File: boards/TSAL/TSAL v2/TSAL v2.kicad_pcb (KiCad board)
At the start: 2 copper layers, 25 parts, among them J1 Ultrafit_2, J2 Ultrafit_2, J3 micromatch_female_RA_4, Q1 NMOS_GSD_30V, U1 LR8K4-G, U2 ZXRE160, U3 MCP6001RT, U4 LTV-356T

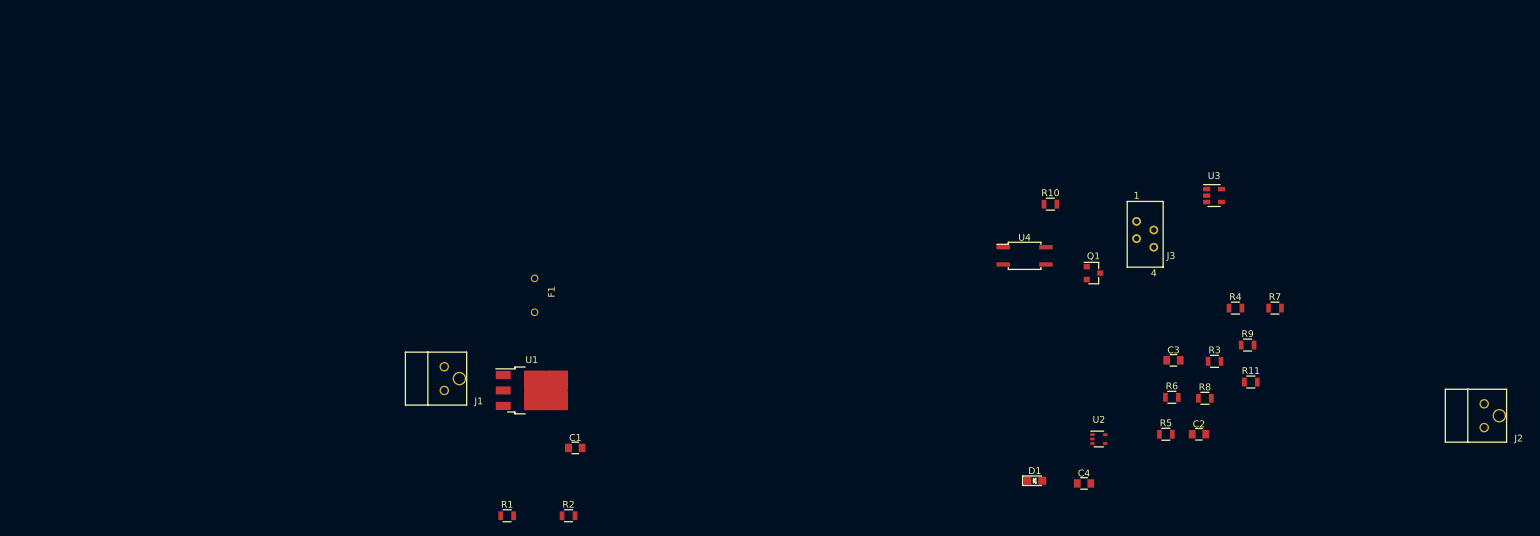
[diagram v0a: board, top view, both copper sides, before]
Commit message: Adding TSAL v2 final schematic
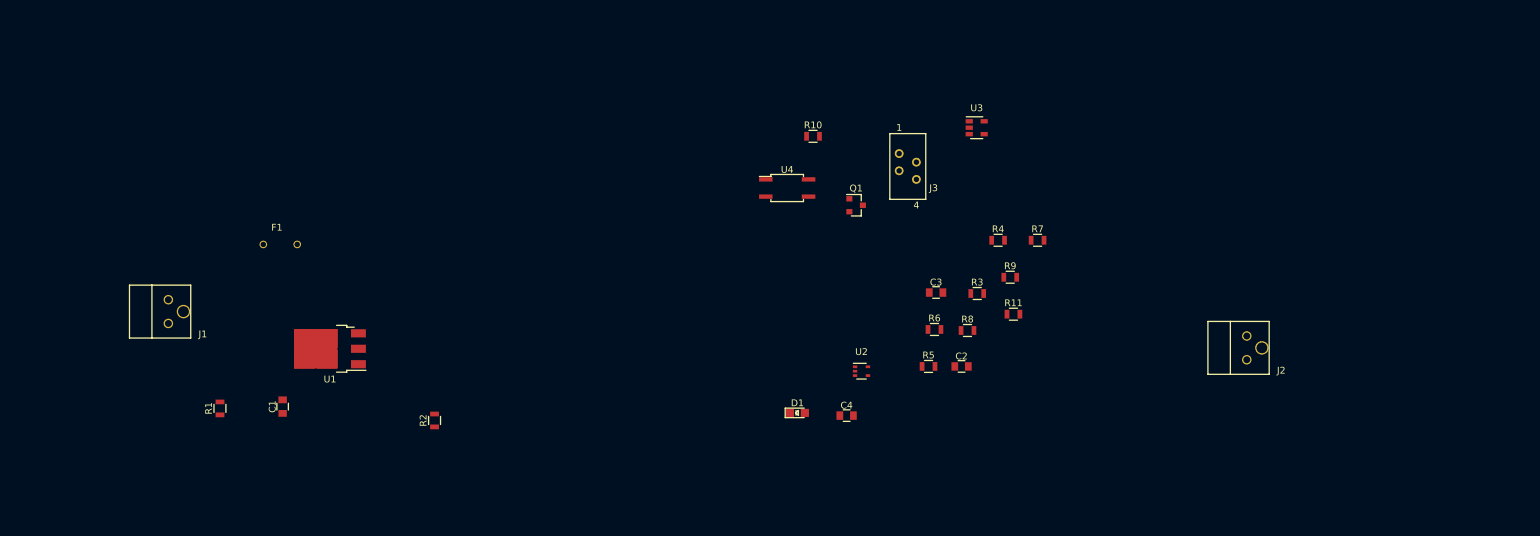
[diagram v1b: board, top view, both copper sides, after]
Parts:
- moved R1 45.2 mm to (73.6, 119.2), turned to 90 degrees
- moved C1 43.6 mm to (82.8, 118.9), turned to 90 degrees
- moved J1 41.9 mm to (66.0, 103.2)
- moved C4 36.4 mm to (166.0, 120.2)
- moved D1 36.4 mm to (158.7, 119.8)
- moved C2 36.4 mm to (182.9, 113.0)
- moved C3 36.4 mm to (179.2, 102.1)
- moved F1 36.4 mm to (85.0, 95.0), turned to 180 degrees
- moved J2 36.4 mm to (225.0, 108.5)
- moved J3 36.4 mm to (173.8, 86.7)
- moved Q1 36.4 mm to (167.4, 89.2)
- moved R10 36.4 mm to (161.1, 79.1)
- moved R11 36.4 mm to (190.6, 105.3)
- moved R3 36.4 mm to (185.3, 102.2)
- moved R4 36.4 mm to (188.3, 94.4)
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
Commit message: BOM, Netlist, PCB final
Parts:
- added G***: LOGO, footprints:Olin_O, B.Cu at (50.8, 72.4)
- added G***: LOGO, footprints:Logo_Large, B.Cu at (80.0, 99.1)
- J3: value micromatch_female_RA_4 -> micromatch_female_TOP_ENTRY_locking_4; footprint footprints:micromatch_female_ra_4 -> footprints:micromatch_female_vert_4
- moved J2 152.5 mm to (73.0, 96.0), turned to 180 degrees
- moved R7 137.1 mm to (57.1, 98.7), turned to 90 degrees
- moved R4 136.3 mm to (52.1, 94.0), turned to 270 degrees
- moved R3 133.2 mm to (52.1, 98.7), turned to 270 degrees
- moved U3 125.2 mm to (61.0, 93.8), turned to 270 degrees
- moved R9 123.7 mm to (67.0, 88.0)
- moved R11 123.6 mm to (71.9, 70.7)
- moved R6 122.6 mm to (57.1, 94.0), turned to 90 degrees
- moved R5 118.0 mm to (61.0, 98.7), turned to 90 degrees
- moved R8 111.6 mm to (72.4, 101.6)
- moved J3 108.5 mm to (66.8, 68.2), turned to 90 degrees
- moved C3 105.6 mm to (73.7, 104.4), turned to 270 degrees
- moved C4 102.9 mm to (66.5, 93.9), turned to 90 degrees
- moved R10 102.4 mm to (59.2, 89.2), turned to 270 degrees
- moved C2 102.2 mm to (81.3, 102.4), turned to 90 degrees
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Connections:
- C1 pad 2: GND -> TS-
- U4 pad 4: VCC -> GLV+
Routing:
- net TS-: track 0.00 -> 105.9 mm, vias 0 -> 2
- net /5V_TS: track 0.00 -> 41.0 mm, vias 0 -> 25
- net Net-(R8-Pad2): track 0.00 -> 23.4 mm, vias 0 -> 2
- net Net-(D1-Pad2): track 0.00 -> 17.1 mm
- net TS+: track 0.00 -> 14.4 mm
- net Net-(R5-Pad1): track 0.00 -> 13.2 mm
- net GLV+: track 0.00 -> 11.2 mm
- net Net-(R10-Pad1): track 0.00 -> 10.4 mm
- net Net-(Q1-Pad1): track 0.00 -> 9.41 mm
- net Net-(F1-Pad2): track 0.00 -> 9.25 mm
- net TSAL-: track 0.00 -> 6.61 mm
- net Net-(R1-Pad1): track 0.00 -> 5.99 mm
- net GND: track 0.00 -> 5.96 mm, vias 0 -> 1
- net Net-(R4-Pad1): track 0.00 -> 5.08 mm
- net Net-(D1-Pad1): track 0.00 -> 3.96 mm
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- added copper zone on B.Cu, net /5V_TS
- added copper zone on B.Cu, net GND
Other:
- board outline added: 40.6 x 58.4 mm
- net class Default: clearance 0.2 -> 0.1524; trace_width 0.25 -> 0.254; via_dia 0.6 -> 0.6096; via_drill 0.4 -> 0.3048
- rule trace_clearance: 0.2 -> 0.1524
- rule via_min_drill: 0.3 -> 0.3048
- rule via_min_size: 0.4 -> 0.6096
- board text added: "HV"
- board text added: "LV"
- board text added: "TS-"
- board text added: "TSAL Rev 2.0 Utsav Gupta 2/5/2018"

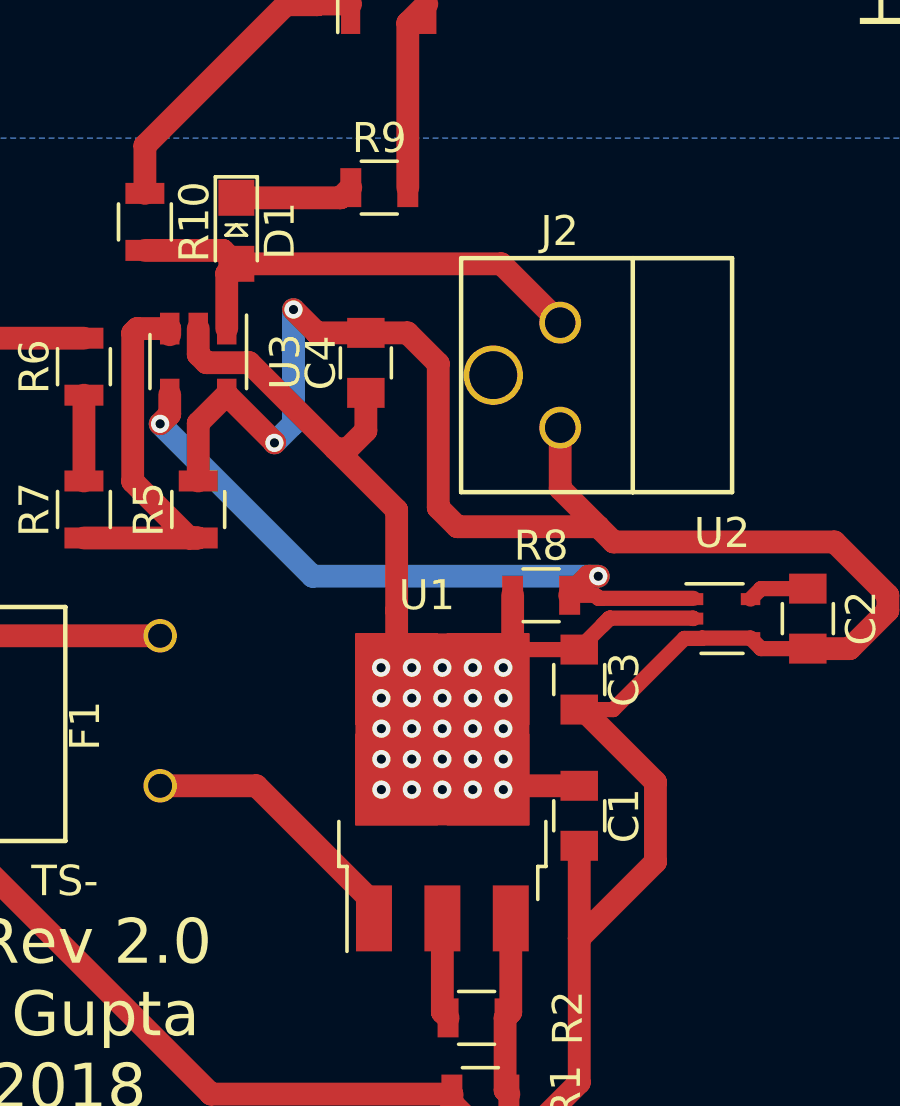
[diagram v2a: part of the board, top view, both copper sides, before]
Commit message: Solved 2 errors
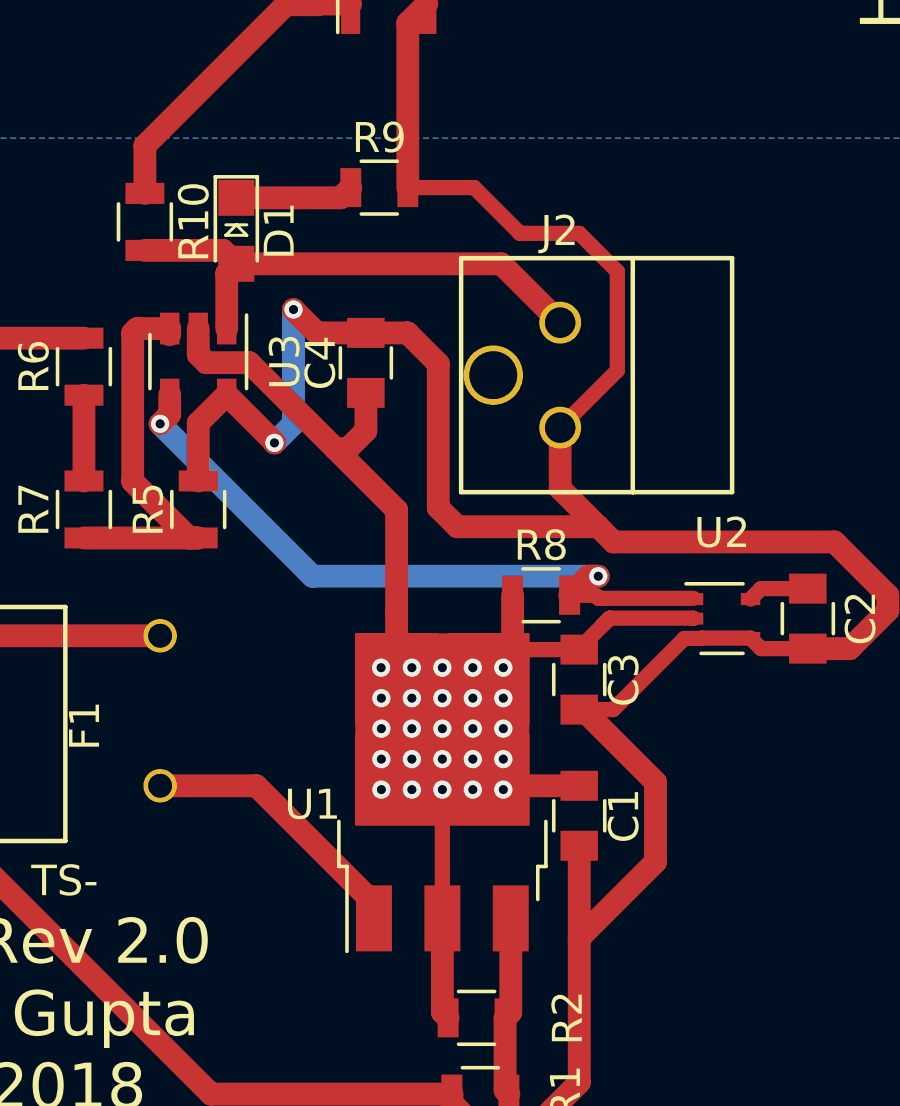
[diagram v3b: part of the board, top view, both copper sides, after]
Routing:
- net TS-: track 105.9 -> 120.1 mm
- net /5V_TS: track 41.0 -> 45.2 mm
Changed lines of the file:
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@@
   (general
     (links 49)
-    (no_connects 5)
+    (no_connects 0)
     (area 42.644287 59.102172 90.170001 123.190001)
     (thickness 1.6)
     (drawings 14)
-    (tracks 157)
+    (tracks 165)
     (zones 0)
     (modules 27)
@@
   )
   (setup
-    (last_trace_width 0.762)
+    (last_trace_width 0.508)
     (user_trace_width 0.254)
     (user_trace_width 0.508)
@@
     (tags "DPAK TO-252 DPAK-3 TO-252-3 SOT-428")
     (attr smd)
-    (fp_text reference U1 (at 6.569335 -0.517787 180) (layer F.SilkS)
+    (fp_text reference U1 (at -0.415665 -4.327787 180) (layer F.SilkS)
       (effects (font (size 1 1) (thickness 0.15)))
     )
@@
   (gr_line (start 46.99 121.92) (end 85.09 121.92) (layer Edge.Cuts) (width 0.15))
   (gr_line (start 45.72 64.77) (end 45.72 120.65) (layer Edge.Cuts) (width 0.15))
+  (segment (start 69.097787 112.369335) (end 69.097787 108.078335) (width 0.508) (layer F.Cu) (net 1))
+  (segment (start 69.097787 108.078335) (end 69.096787 108.077335) (width 0.508) (layer F.Cu) (net 1))
   (segment (start 62.661721 93.846599) (end 65.532 96.716878) (width 0.762) (layer F.Cu) (net 1))
   (segment (start 65.532 96.716878) (end 67.572787 98.757665) (width 0.762) (layer F.Cu) (net 1))
@@
   (via (at 74.93 69.85) (size 0.6096) (drill 0.3048) (layers F.Cu B.Cu) (net 2))
   (segment (start 72.898 70.739) (end 72.898 67.183) (width 0.762) (layer F.Cu) (net 2))
+  (segment (start 74.93 90.805) (end 74.93 94.107) (width 0.508) (layer F.Cu) (net 3))
+  (segment (start 74.93 94.107) (end 73.025 96.012) (width 0.508) (layer F.Cu) (net 3))
+  (segment (start 73.66 89.535) (end 74.93 90.805) (width 0.508) (layer F.Cu) (net 3))
+  (segment (start 71.683254 89.535) (end 73.66 89.535) (width 0.508) (layer F.Cu) (net 3))
+  (segment (start 67.945 88.011) (end 70.159254 88.011) (width 0.508) (layer F.Cu) (net 3))
+  (segment (start 70.159254 88.011) (end 71.683254 89.535) (width 0.508) (layer F.Cu) (net 3))
   (segment (start 63.5 96.52) (end 63.5 96.5) (width 0.762) (layer F.Cu) (net 3))
   (segment (start 63.5 96.5) (end 61.91 94.91) (width 0.762) (layer F.Cu) (net 3))

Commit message: Hopefully finalised
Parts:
- moved G*** 5.72 mm to (80.0, 93.3)
- moved G*** 5.24 mm to (49.5, 77.5)
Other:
- outline, holes or cut-outs redrawn
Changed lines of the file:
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@@
     (area 42.644287 59.102172 90.170001 123.190001)
     (thickness 1.6)
-    (drawings 14)
+    (drawings 18)
     (tracks 165)
     (zones 0)
@@
       (effects (font (size 1 1) (thickness 0.15)))
     )
-    (fp_text value NMOS_GSD_30V (at -0.03 -2.55 90) (layer F.Fab)
+    (fp_text value NMOS_GSD_30V (at -3.032 -16.068 90) (layer F.Fab)
       (effects (font (size 1 1) (thickness 0.15)))
     )
@@
   )
   (module footprints:Olin_O (layer B.Cu)
-    (at 50.8 72.39 90)
+    (at 49.53 77.47 90)
     (fp_text reference G*** (at 10.16 5.08 90) (layer B.SilkS) hide
       (effects (font (thickness 0.3)) (justify mirror))
@@
   )
   (module footprints:Logo_Large (layer B.Cu)
-    (at 80.01 99.06 270)
+    (at 80.01 93.345 270)
     (fp_text reference G*** (at 0 0 270) (layer B.SilkS) hide
       (effects (font (thickness 0.3)) (justify mirror))
@@
       (xy 18.232145 4.0226) (xy 18.481106 4.090329) (xy 18.746513 4.111367) (xy 18.846075 4.107132)) (layer B.SilkS) (width 0.01))
   )
+  (gr_arc (start 81.28 117.285008) (end 81.28 121.285) (angle -90) (layer Edge.Cuts) (width 0.1))
+  (gr_line (start 48.639984 121.285) (end 81.28 121.285) (layer Edge.Cuts) (width 0.1))
+  (gr_arc (start 81.28 66.864992) (end 85.279992 66.864992) (angle -90) (layer Edge.Cuts) (width 0.1))
+  (gr_arc (start 48.639984 66.864992) (end 48.639984 62.865) (angle -90) (layer Edge.Cuts) (width 0.1))
+  (gr_line (start 85.279992 117.285008) (end 85.279992 66.864992) (layer Edge.Cuts) (width 0.1))
+  (gr_arc (start 48.639984 117.285008) (end 44.639992 117.285008) (angle -90) (layer Edge.Cuts) (width 0.1))
+  (gr_circle (center 48.639984 117.285008) (end 48.639984 115.285012) (layer Edge.Cuts) (width 0.1))
+  (gr_circle (center 48.639984 66.864992) (end 48.639984 64.864996) (layer Edge.Cuts) (width 0.1))
+  (gr_circle (center 81.28 117.285008) (end 81.28 115.285012) (layer Edge.Cuts) (width 0.1))
+  (gr_line (start 44.639992 66.864992) (end 44.639992 117.285008) (layer Edge.Cuts) (width 0.1))
+  (gr_circle (center 81.28 66.864992) (end 81.28 64.864996) (layer Edge.Cuts) (width 0.1))
+  (gr_line (start 81.28 62.865) (end 48.639984 62.865) (layer Edge.Cuts) (width 0.1))
   (gr_text TS- (at 56.515 111.125) (layer F.SilkS)
     (effects (font (size 1.016 1.016) (thickness 0.254)))
   )
-  (gr_text "TSAL Rev 2.0\nUtsav Gupta\n2/5/2018\n" (at 54.61 115.57) (layer F.SilkS)
+  (gr_text "TSAL Rev 2.0\nUtsav Gupta\n2/5/2018\n" (at 57.785 116.205) (layer F.SilkS)
     (effects (font (size 1.5 1.5) (thickness 0.3)))
   )
-  (gr_arc (start 46.99 120.65) (end 46.99 121.92) (angle 90) (layer Edge.Cuts) (width 0.15))
-  (gr_arc (start 85.09 120.65) (end 86.36 120.65) (angle 90) (layer Edge.Cuts) (width 0.15))
-  (gr_arc (start 85.09 64.77) (end 85.09 63.5) (angle 90) (layer Edge.Cuts) (width 0.15))
-  (gr_arc (start 46.99 64.77) (end 45.72 64.77) (angle 90) (layer Edge.Cuts) (width 0.15))
   (dimension 12.7 (width 0.3) (layer F.SilkS)
     (gr_text "0.5000 in" (at 48.18 78.563549 270) (layer F.SilkS)
@@
     (effects (font (size 1.5 1.5) (thickness 0.3)))
   )
-  (gr_line (start 48.26 78.74) (end 86.36 78.74) (layer F.SilkS) (width 0.2))
-  (gr_line (start 85.09 63.5) (end 46.99 63.5) (layer Edge.Cuts) (width 0.15))
-  (gr_line (start 86.36 120.65) (end 86.36 64.77) (layer Edge.Cuts) (width 0.15))
-  (gr_line (start 46.99 121.92) (end 85.09 121.92) (layer Edge.Cuts) (width 0.15))
-  (gr_line (start 45.72 64.77) (end 45.72 120.65) (layer Edge.Cuts) (width 0.15))
+  (gr_line (start 46.355 78.74) (end 84.455 78.74) (layer F.SilkS) (width 0.2))
   (segment (start 69.097787 112.369335) (end 69.097787 108.078335) (width 0.508) (layer F.Cu) (net 1))
   (segment (start 69.097787 108.078335) (end 69.096787 108.077335) (width 0.508) (layer F.Cu) (net 1))

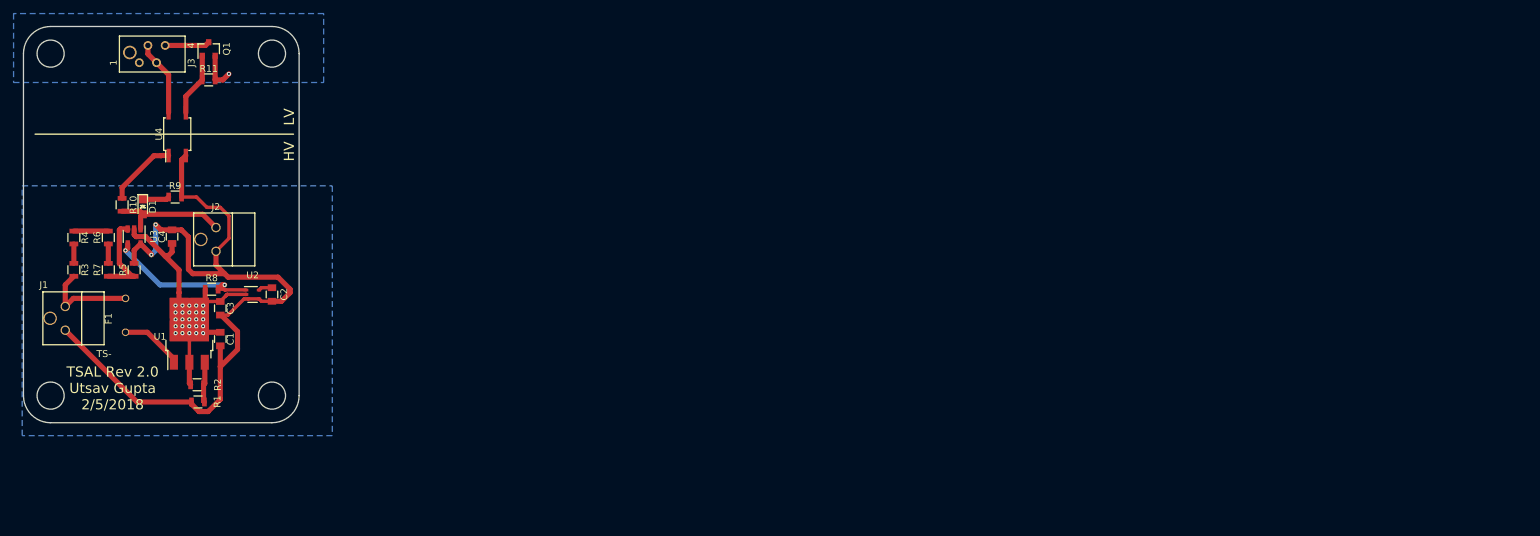
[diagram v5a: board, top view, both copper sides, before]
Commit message: Added 1.43k res for AIL
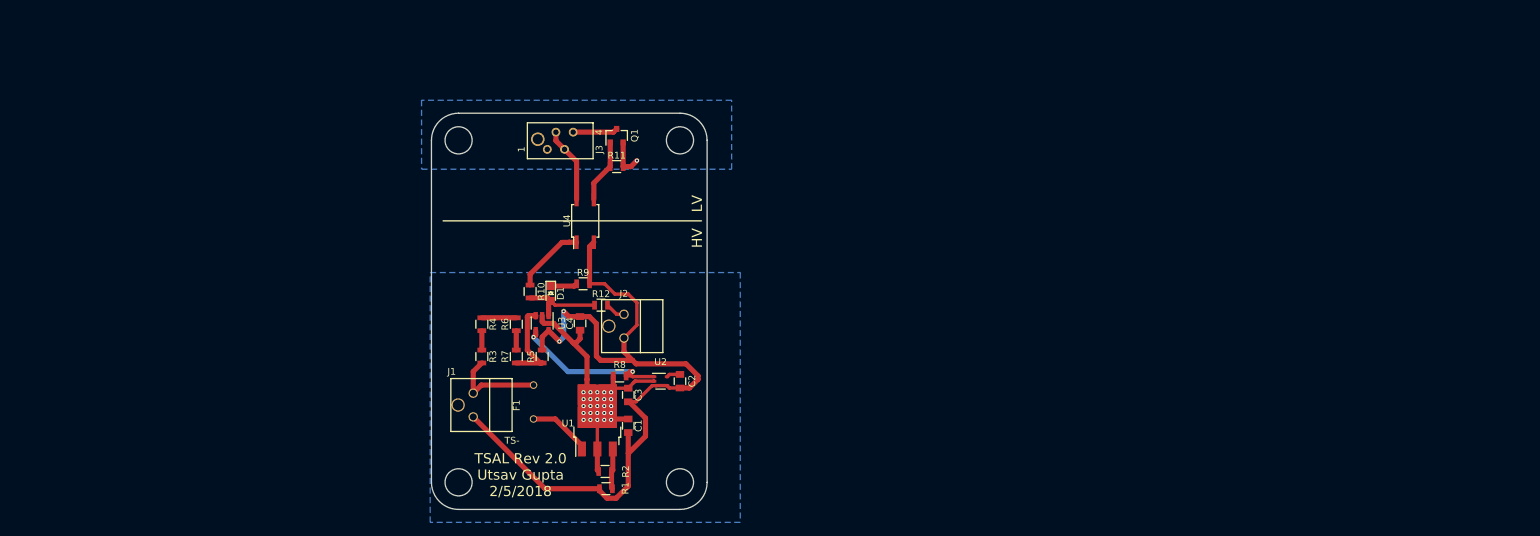
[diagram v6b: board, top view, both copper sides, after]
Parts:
- added R12: R_1.43k, footprints:R_0805_OEM, F.Cu at (129.8, 103.9)
- moved R11 61.5 mm to (132.1, 83.5)
- moved R2 61.5 mm to (130.4, 128.5)
- moved R8 61.5 mm to (132.5, 114.4)
- moved U1 61.5 mm to (129.2, 121.0)
- moved D1 61.5 mm to (122.4, 102.2)
- moved R3 61.5 mm to (112.2, 111.5)
- moved R4 61.5 mm to (112.2, 106.8)
- moved R6 61.5 mm to (117.3, 106.8)
- moved R7 61.5 mm to (117.3, 111.5)
- moved C1 61.5 mm to (133.8, 121.7)
- moved C2 61.5 mm to (141.4, 115.2)
- moved C3 61.5 mm to (133.8, 117.2)
- moved C4 61.5 mm to (126.7, 106.6)
- moved F1 61.5 mm to (119.8, 115.7)
- moved G*** 61.5 mm to (109.7, 90.3)
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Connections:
- J2 pad 1: Net-(D1-Pad2) -> Net-(J2-Pad1)
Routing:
- net Net-(D1-Pad2): track 17.1 -> 12.2 mm
- net Net-(J2-Pad1): track 0.00 -> 2.99 mm

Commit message: Forgot to save the file
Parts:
- moved Q1 59.3 mm to (178.1, 116.4), turned to 0 degrees
- moved J3 57.7 mm to (176.1, 111.2), turned to 0 degrees
- moved G*** 57.2 mm to (166.8, 94.0), turned to 0 degrees
- moved R11 52.9 mm to (173.5, 116.4), turned to 270 degrees
- moved U4 43.1 mm to (165.5, 111.7), turned to 0 degrees
- moved R4 39.4 mm to (150.3, 96.5), turned to 180 degrees
- moved R3 36.5 mm to (145.5, 96.5), turned to 180 degrees
- moved J1 36.0 mm to (136.6, 95.2), turned to 90 degrees
- moved R10 35.8 mm to (155.1, 103.6), turned to 180 degrees
- moved R6 33.4 mm to (150.3, 101.6), turned to 0 degrees
- moved D1 32.7 mm to (154.8, 106.7), turned to 180 degrees
- moved R9 31.0 mm to (156.3, 111.4), turned to 270 degrees
- moved R7 29.9 mm to (145.5, 101.6), turned to 0 degrees
- moved U3 29.4 mm to (150.5, 105.4), turned to 180 degrees
- moved R12 25.4 mm to (153.1, 114.1), turned to 270 degrees
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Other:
- board size 40.6 x 58.4 mm -> 58.4 x 40.6 mm
